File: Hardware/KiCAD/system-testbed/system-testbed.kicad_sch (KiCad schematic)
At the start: 25 parts, among them J1 Stemma QT, J7 Stemma QT, J8 Stemma QT, X1 EYESPI, X11 EYESPI, X6 EYESPI, X7 EYESPI, X8 EYESPI, X9 EYESPI

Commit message: feat: update pinouts for mcu #53
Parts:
- added X2, X3: EYESPI, capstone-project:Adafruit EYESPI FPC Connector, symbol capstone-project:Adafruit EYESPI FPC Connector
- X9: Assignment PSU_I2C+INT -> AUDIO_I2S
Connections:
- net +3.3V: now also X1.16, X1.2, X1.7, X6.16, X6.2, X6.7, X8.16, X8.2, X8.7, X2.1, X3.1, X3.16, X3.2, X3.7
- net AMP_DIN: now also X9.12, X2.12; no longer X9.13
- net BCLK: now also X9.17, X2.17; no longer X9.10
- net GND: now also X1.10, X1.11, X1.12, X6.10, X6.11, X6.12, X8.10, X8.11, X8.12, X8.3, X8.Z1, X8.Z2, X9.3, X9.Z1, X9.Z2, X2.3, X2.Z1, X2.Z2, X3.10, X3.11, X3.12, X3.3, X3.Z1, X3.Z2
- net LRCLK: now also X9.18, X2.18; no longer X9.11
- net MIC_DOUT: now also X9.11, X2.11; no longer X9.12
- net SCL: now also X6.14, X7.14, X9.13, X2.13, X3.13
- net SDA: now also X6.13, X7.13, X9.14, X2.14, X3.14
- net ~{AMP_SD}: now also X2.10
- net AUDIO_INT: now reaches X9.15
- net AUDIO_INT: now also X2.15
- net RXD0: now reaches X8.17
- net RXD0: now also X3.17
- net TXD0: now reaches X8.18
- net TXD0: now also X3.18
- net RF_INT: now reaches X6.15
- net HMI_INT: now reaches X7.15
- net MCU/BMS_INT renamed BMS_INT
- net BMS_INT: now also X3.15
- no-connect marks 0 -> 51
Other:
- sheet MCU ports: added RXD0, TXD0; removed none
- sheet Power Subsystem ports: added *INT; removed Vsys
- sheet RF Subsystem ports: added none; removed PA_{SHUTDOWN}, TRX_GPIO3
- note added: "Audio Modulino"
- note added: "Battery Modulino BMS on I2C0 @ 0x6B"
- note added: "CC1200 on VSPI Unused I2C0+INT RX Switch on ??? 4x 3.3V return paths"
- note added: "Display on HSPI: SD Card Unused Port Expander on I2C0+INT @ ???"
- note added: "ESP32 Modulino X? EYESPI to Modulino Nodes"
- note added: "Human-Machine Interface Modulino"
- note added: "Mic+Amp on I2S0: MAX98357A IO36 INPUT ICS-43434 IO33 OUTPUT Unused I2C0+INT"
- note added: "RF Modulino"
- note removed: "Battery Modulino BMS on I2C @ addr"
- note removed: "ESP32 Module"
- note removed: "RF Modulino CC1200 on VSPI"
- note removed: "TODO: Can TRX_GPIO0 and TRX_GPIO2 be on pins 17 and 18 of EYESPI FPC? How many pins can be safely reused on EYESPI FPC for the TI CC1200?"
- moved on the sheet: H1, H10, H11, H12, H13, H14, H15, H16, H2, H3, H4, H5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

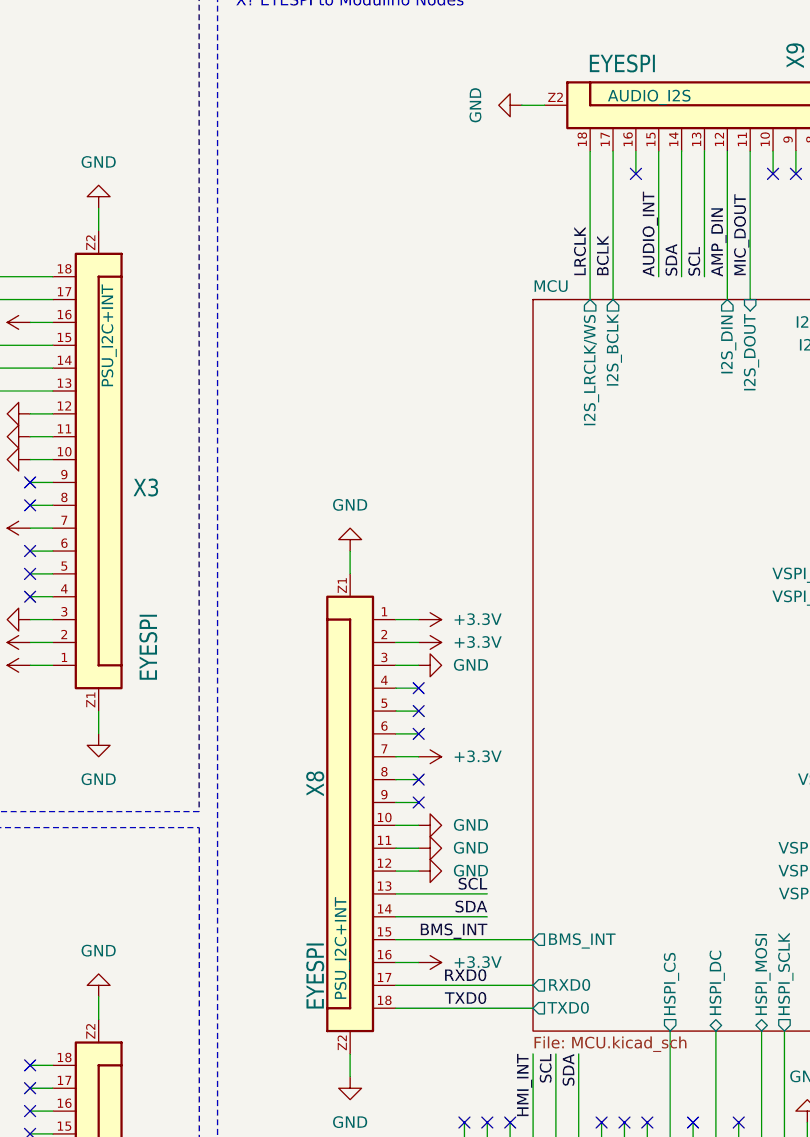
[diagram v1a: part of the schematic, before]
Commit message: feat: separate RF subsystems for testing using SMA edge launches in testbed KiCAD project #65 #34 #45
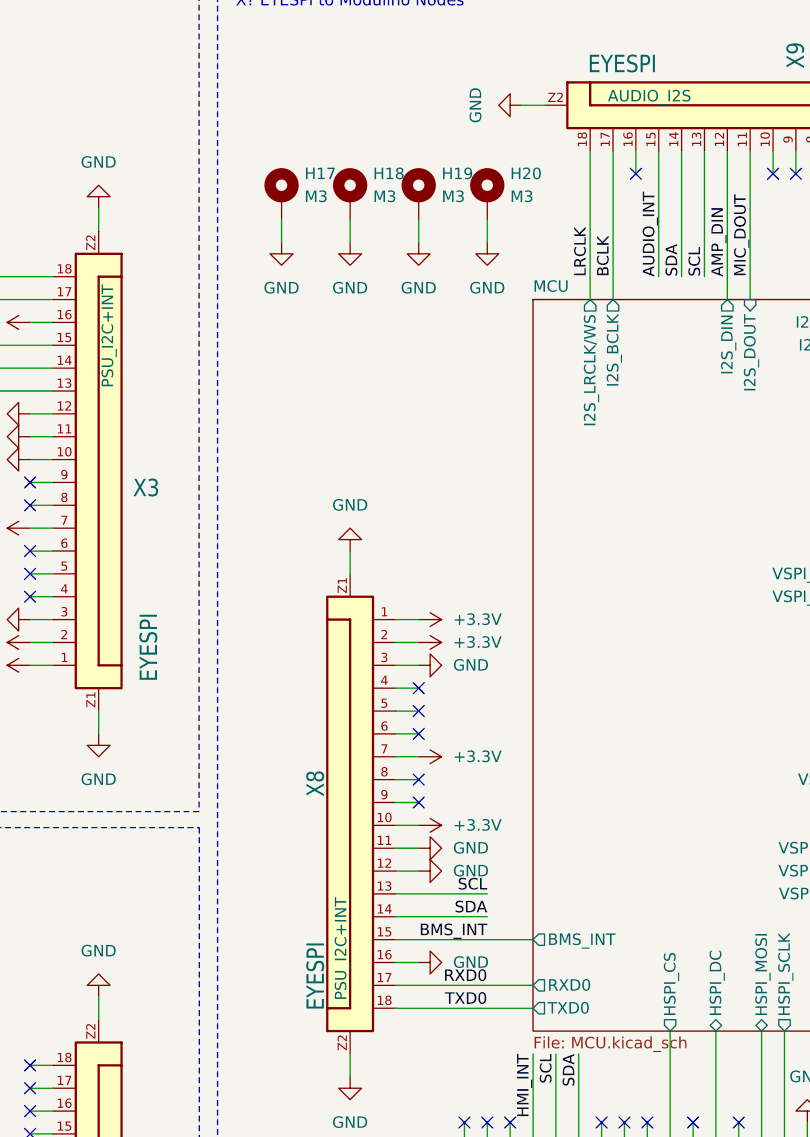
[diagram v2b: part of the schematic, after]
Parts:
- added H17, H18, H19, H20: M3, MountingHole:MountingHole_3.2mm_M3_ISO14580_Pad, symbol Mechanical:MountingHole_Pad
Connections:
- net +3.3V: now also X8.10; no longer X8.16
- net GND: now also X8.16, H17.1, H18.1, H19.1, H20.1; no longer X8.10
